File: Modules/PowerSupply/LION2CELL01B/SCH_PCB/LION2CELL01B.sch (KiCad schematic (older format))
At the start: 96 parts, among them J1 JUMP_4X2, J10 JUMP_2x1, J11 JUMP_2x1, J12 JUMP_2x1, J13 JUMP_4X2, J14 JUMP_2x1, J2 JUMP_2x1, J3 JUMP_2x1, J4 JUMP_2x1, J5 JUMP_2x1, J6 JUMP_2x1, J7 JUMP_4X2, J8 CONN1_1, J9 CONN1_1, P1 _, P2 _, P3 _, P4 _, Q1 IRLML6244, Q2 MMBF170LT1G, Q3 MMBF170LT1G, Q4 BSS83P, SW1 SW_PUSH, U1 BQ29209, U2 BQ24103, U3 BQ34Z100, U4 SN74HC164D

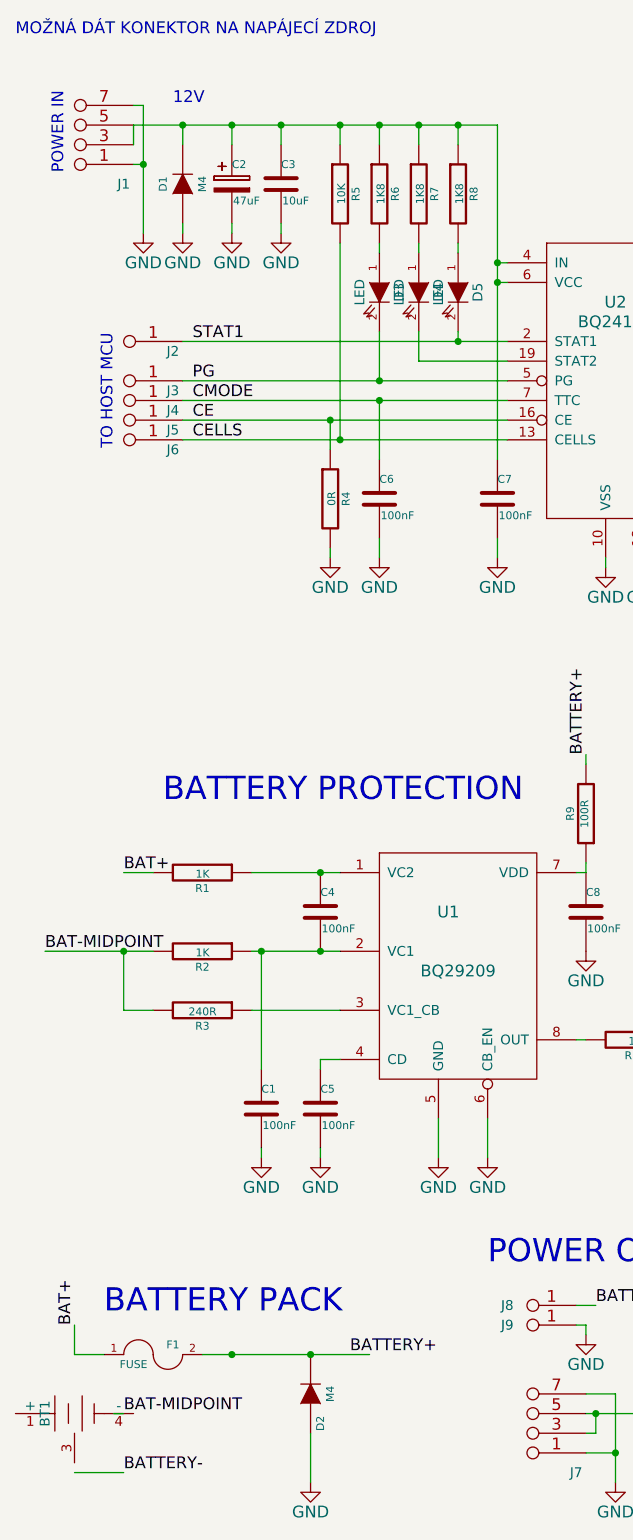
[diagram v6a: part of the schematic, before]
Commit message: 
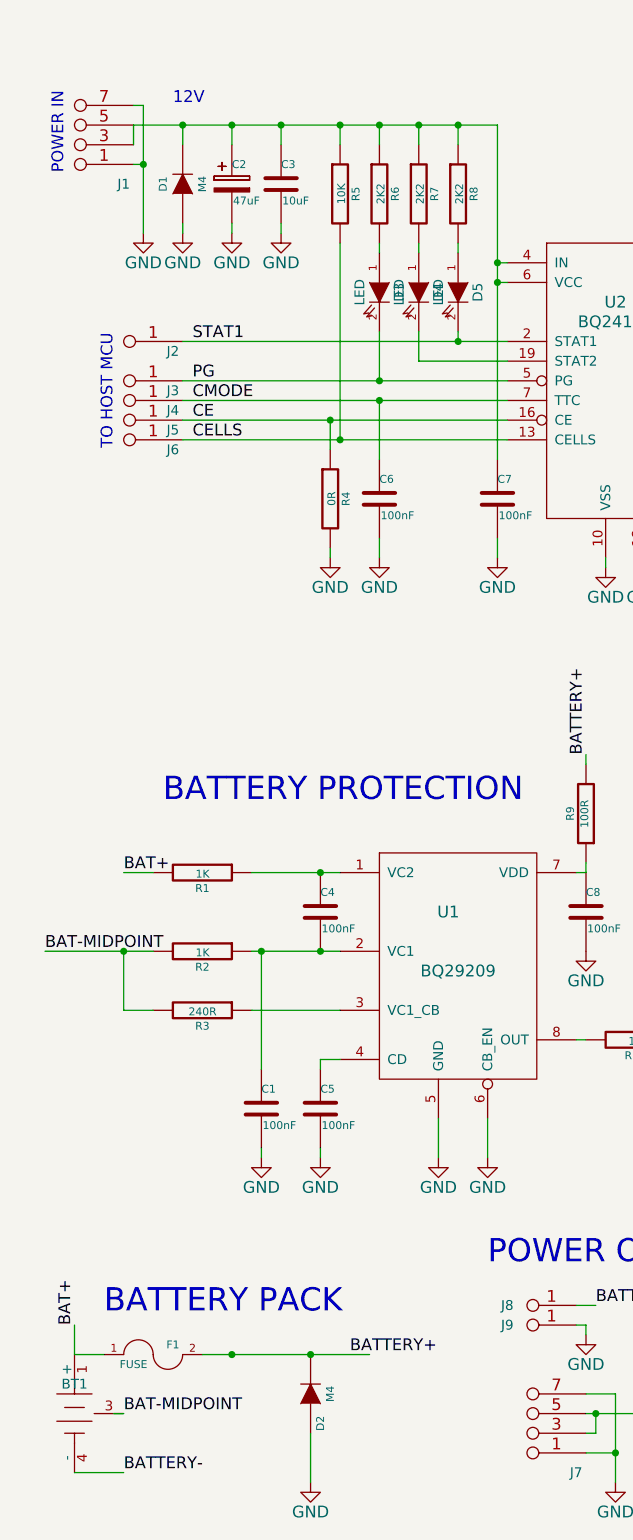
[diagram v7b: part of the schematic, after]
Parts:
- R6, R7, R8: value 1K8 -> 2K2
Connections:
- net BAT+: now also BT1.1 (+)
- net BAT-MIDPOINT: now also BT1.2, BT1.3
- net BATTERY-: now also BT1.4 (-)
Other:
- note removed: "MOŽNÁ DÁT KONEKTOR NA NAPÁJECÍ ZDROJ"
- moved on the sheet: BT1
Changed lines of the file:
@@
 P 2250 1050
 F 0 "R6" V 2330 1050 40  0000 C CNN
-F 1 "1K8" V 2257 1051 40  0000 C CNN
+F 1 "2K2" V 2257 1051 40  0000 C CNN
 F 2 "Mlab_R:SMD-0805" V 2180 1050 30  0001 C CNN
 F 3 "" H 2250 1050 30  0000 C CNN
@@
 P 2450 1050
 F 0 "R7" V 2530 1050 40  0000 C CNN
-F 1 "1K8" V 2457 1051 40  0000 C CNN
+F 1 "2K2" V 2457 1051 40  0000 C CNN
 F 2 "Mlab_R:SMD-0805" V 2380 1050 30  0001 C CNN
 F 3 "" H 2450 1050 30  0000 C CNN
@@
 P 2650 1050
 F 0 "R8" V 2730 1050 40  0000 C CNN
-F 1 "1K8" V 2657 1051 40  0000 C CNN
+F 1 "2K2" V 2657 1051 40  0000 C CNN
 F 2 "Mlab_R:SMD-0805" V 2580 1050 30  0001 C CNN
 F 3 "" H 2650 1050 30  0000 C CNN
@@
 F 3 "" H 2300 7600 60  0000 C CNN
 	1    700  7250
-	1    0    0    -1
+	0    -1   1    0
 $EndComp
 $Comp
@@
 Text Notes 1200 600  0    60   ~ 0
 12V
-Text Notes 400  250  0    60   ~ 0
-MOŽNÁ DÁT KONEKTOR NA NAPÁJECÍ ZDROJ
 $Comp
 L R R10
